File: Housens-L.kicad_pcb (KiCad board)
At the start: 4 copper layers, 50 x 50 mm, 45 parts, among them J1 JTAG/SWD, J2 USB_C_2.0, Q1 DMC3071LVT, SW1 RESET, SW2 USER_BTN, U1 MCP1603, U2 BME280, U3 OPT3005, U4 STM32WB55CGUx, Y1 32MHz, Y2 32.768kHz

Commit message: Layout JTAG
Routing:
- net /JTDI: track 0.61 -> 19.5 mm, vias 1 -> 2
- net /JTRST: track 0.61 -> 19.2 mm, vias 1 -> 2
- net /SWTRACE_JTDO: track 0.61 -> 18.5 mm, vias 1 -> 2
- net /SWCLK_JTCK: track 0.61 -> 18.4 mm, vias 1 -> 2
- net /SWDIO_JTMS: track 0.62 -> 18.2 mm, vias 1 -> 2

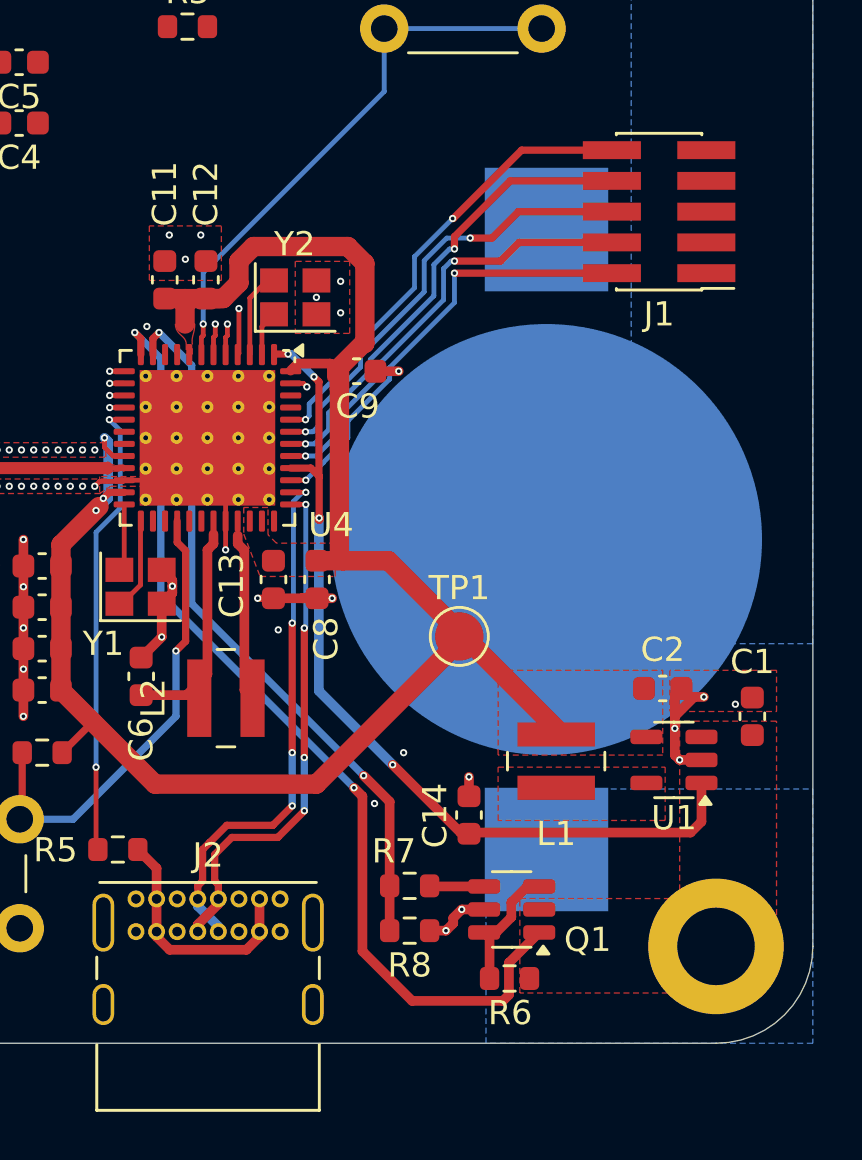
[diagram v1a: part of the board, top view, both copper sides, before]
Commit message: Add 3D model for cell holder
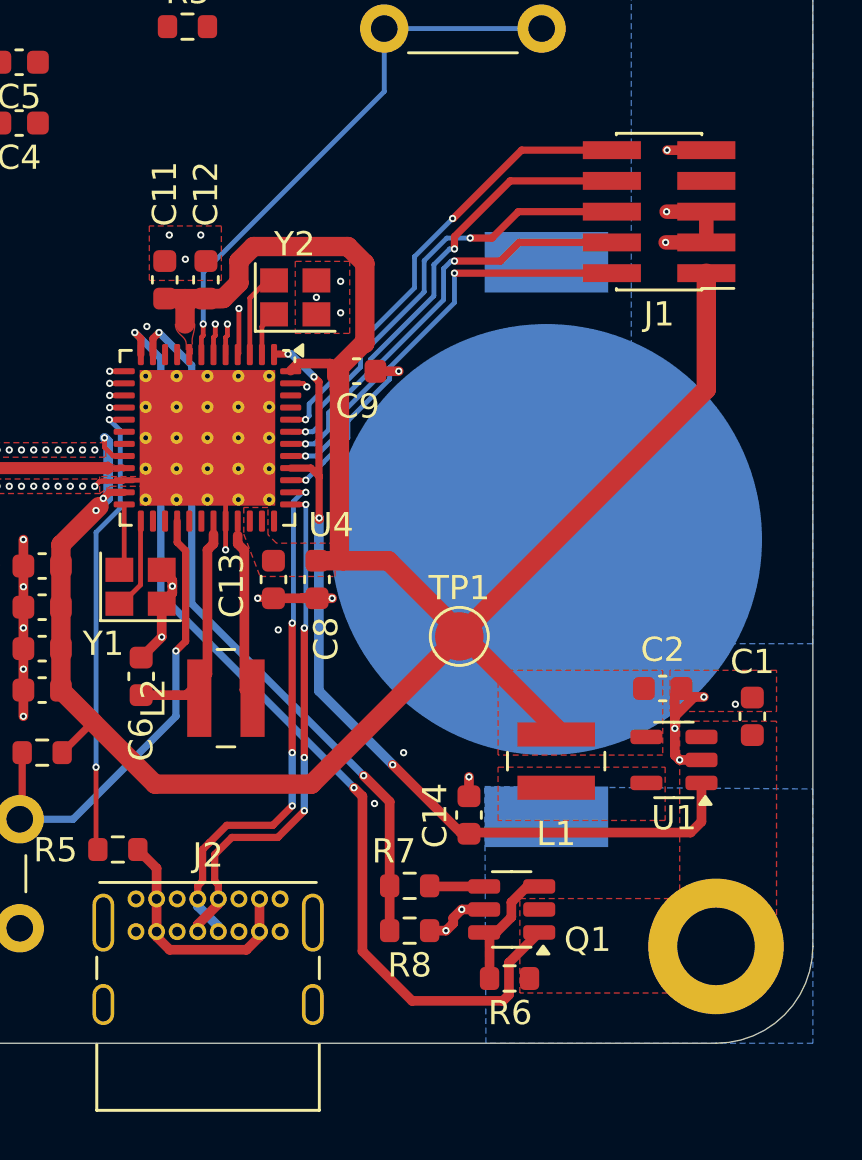
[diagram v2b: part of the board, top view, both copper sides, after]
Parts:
- BT1: footprint Battery:BatteryHolder_Keystone_3002_1x2032 -> Invented:BAT-HLD-001_3Pins
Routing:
- net +1V8: track 77.9 -> 96.9 mm
- net GND: track 36.5 -> 42.7 mm, vias 110 -> 113

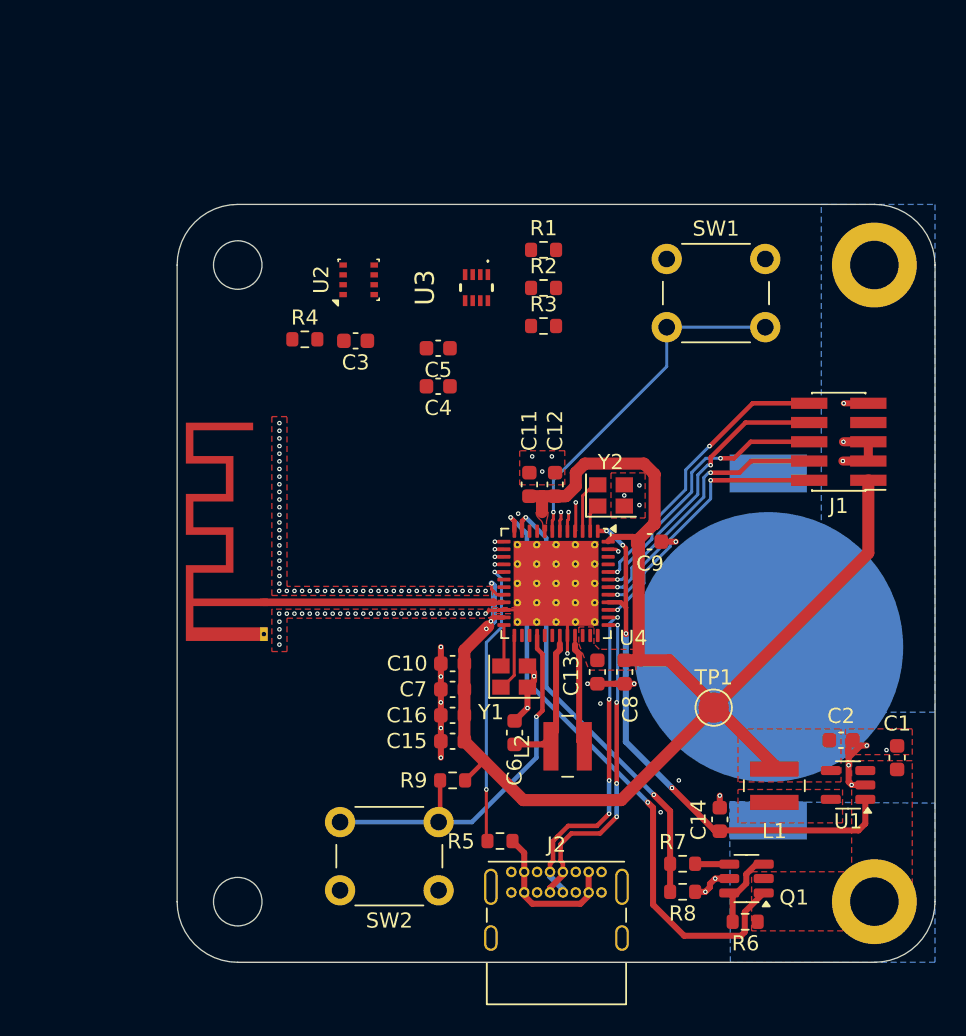
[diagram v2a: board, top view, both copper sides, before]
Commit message: Show some labels
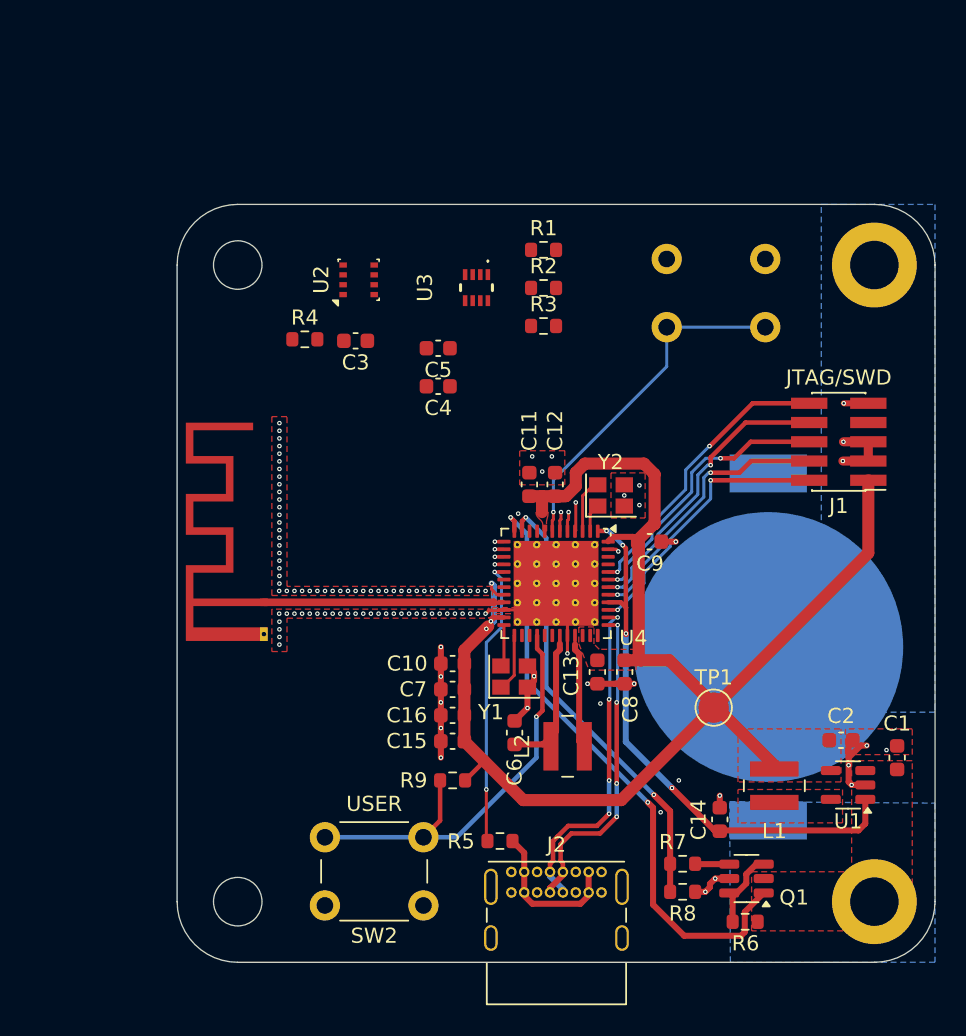
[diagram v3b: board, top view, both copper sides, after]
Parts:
- SW1: moved to B.Cu
- SW2: value USER_BTN -> USER
- moved SW1 6.50 mm to (98.8, 83.6), turned to 180 degrees
- moved SW2 1.41 mm to (76.2, 126.2)
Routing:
- net /USER_BTN: track 25.9 -> 28.7 mm

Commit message: Layout BME280
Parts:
- moved R2 27.7 mm to (59.2, 73.5)
- moved R1 27.7 mm to (59.2, 71.0)
- moved R3 27.7 mm to (59.2, 76.0)
- moved U3 27.7 mm to (54.8, 73.5)
- moved C4 27.7 mm to (52.2, 80.0)
- moved C5 27.7 mm to (52.2, 77.5)
- moved R4 17.0 mm to (84.2, 82.7), turned to 90 degrees
- moved C3 15.5 mm to (85.9, 82.7), turned to 90 degrees
- moved U2 13.1 mm to (85.0, 86.0), turned to 180 degrees
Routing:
- net +1V8: track 96.9 -> 113.7 mm
- net GND: track 42.7 -> 46.8 mm, vias 113 -> 116
- net /SPI1_MISO: track 0.60 -> 2.16 mm

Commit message: Layout I2C
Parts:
- moved SW1 29.2 mm to (72.0, 95.3), turned to -90 degrees
- moved U3 25.8 mm to (76.0, 88.1)
- moved C4 24.8 mm to (76.9, 82.7), turned to 90 degrees
- moved C5 23.5 mm to (75.2, 82.7), turned to 90 degrees
- moved R1 18.0 mm to (68.8, 86.2), turned to -90 degrees
- moved R2 17.0 mm to (70.5, 86.2), turned to -90 degrees
- moved R3 16.6 mm to (72.2, 86.2), turned to -90 degrees
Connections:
- U4 pad 4: /BOOT0 -> GND
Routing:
- net /I2C1_SDA: track 0.73 -> 28.7 mm, vias 1 -> 2
- net /I2C1_SCL: track 1.29 -> 25.3 mm, vias 1 -> 2
- net +1V8: track 113.7 -> 137.0 mm
- net /OPT_INT: track 1.29 -> 21.9 mm, vias 1 -> 2
- net Net-(U4-NRST): track 23.1 -> 16.6 mm
- net GND: track 46.8 -> 51.7 mm, vias 116 -> 122
- net /BOOT0: track 1.92 -> 0.00 mm, vias 1 -> 0

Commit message: Layout SPI
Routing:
- net /SPI1_MISO: track 2.16 -> 22.3 mm, vias 1 -> 0
- net /SPI1_MOSI: track 0.60 -> 18.8 mm, vias 1 -> 2
- net /SPI1_CLK: track 0.60 -> 17.9 mm, vias 1 -> 0
- net /SPI1_NSS: track 0.60 -> 16.9 mm, vias 1 -> 0
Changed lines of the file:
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@@
 	)
 	(via
-		(at 84.2 95.4)
-		(size 0.3)
-		(drill 0.15)
-		(layers "F.Cu" "B.Cu")
-		(remove_unused_layers yes)
-		(keep_end_layers no)
-		(zone_layer_connections "In1.Cu" "In2.Cu")
+		(at 84.1 97.1)
+		(size 0.3)
+		(drill 0.15)
+		(layers "F.Cu" "B.Cu")
+		(remove_unused_layers yes)
+		(keep_end_layers no)
+		(zone_layer_connections "F.Cu" "In1.Cu" "In2.Cu")
 		(net 2)
 	)
@@
 	)
 	(via
-		(at 84.725 96.625)
+		(at 84.6 96.55)
 		(size 0.3)
 		(drill 0.15)
@@
 	)
 	(via
-		(at 84.333364 96.366636)
+		(at 83.593199 96.55)
 		(size 0.3)
 		(drill 0.15)
@@
 	(segment
 		(start 81.5625 102.25)
-		(end 80.9625 102.25)
+		(end 81.437501 102.125001)
 		(width 0.2)
 		(layer "F.Cu")
 		(net 10)
 	)
-	(via
-		(at 80.9625 102.25)
-		(size 0.3)
-		(drill 0.15)
-		(layers "F.Cu" "B.Cu")
-		(remove_unused_layers yes)
-		(keep_end_layers no)
-		(zone_layer_connections)
+	(segment
+		(start 85.35 91.25)
+		(end 85.35 87.05)
+		(width 0.2)
+		(layer "F.Cu")
 		(net 10)
+	)
+	(segment
+		(start 81.437501 102.125001)
+		(end 81.437501 95.162499)
+		(width 0.2)
+		(layer "F.Cu")
+		(net 10)
+	)
+	(segment
+		(start 81.437501 95.162499)
+		(end 85.35 91.25)
+		(width 0.2)
+		(layer "F.Cu")
+		(net 10)
+	)
+	(segment
+		(start 81.984315 94.05)
+		(end 84.7 91.334315)
+		(width 0.2)
+		(layer "F.Cu")
+		(net 11)
+	)
+	(segment
+		(start 80.9625 101.4875)
+		(end 80.9625 95.071815)
+		(width 0.2)
+		(layer "F.Cu")
+		(net 11)
+	)
+	(segment
+		(start 80.9625 95.071815)
+		(end 81.037501 94.996814)
+		(width 0.2)
+		(layer "F.Cu")
+		(net 11)
+	)
+	(segment
+		(start 81.037501 94.996814)
+		(end 81.037501 94.996813)
+		(width 0.2)
+		(layer "F.Cu")
+		(net 11)
+	)
+	(segment
+		(start 84.7 91.334315)
+		(end 84.7 87.05)
+		(width 0.2)
+		(layer "F.Cu")
+		(net 11)
 	)
 	(segment
@@
 		(net 11)
 	)
-	(via
-		(at 80.9625 103.75)
+	(segment
+		(start 81.037501 94.996813)
+		(end 81.984315 94.05)
+		(width 0.2)
+		(layer "F.Cu")
+		(net 11)
+	)
+	(via
+		(at 80.9625 101.4875)
 		(size 0.3)
 		(drill 0.15)
@@
 		(net 11)
 	)
-	(segment
-		(start 80.9625 102.75)
-		(end 81.5625 102.75)
+	(via
+		(at 80.9625 103.75)
+		(size 0.3)
+		(drill 0.15)
+		(layers "F.Cu" "B.Cu")
+		(remove_unused_layers yes)
+		(keep_end_layers no)
+		(zone_layer_connections)
+		(net 11)
+	)
+	(segment
+		(start 80.9625 101.4875)
+		(end 80.9625 103.75)
+		(width 0.2)
+		(layer "B.Cu")
+		(net 11)
+	)
+	(segment
+		(start 81.110614 102.75)
+		(end 80.5125 102.151886)
 		(width 0.2)
 		(layer "F.Cu")
 		(net 12)
 	)
-	(via
-		(at 80.9625 102.75)
-		(size 0.3)
-		(drill 0.15)
-		(layers "F.Cu" "B.Cu")
-		(remove_unused_layers yes)
-		(keep_end_layers no)
-		(zone_layer_connections)
+	(segment
+		(start 80.5125 102.151886)
+		(end 80.5125 94.956129)
+		(width 0.2)
+		(layer "F.Cu")
 		(net 12)
+	)
+	(segment
+		(start 81.5625 102.75)
+		(end 81.110614 102.75)
+		(width 0.2)
+		(layer "F.Cu")
+		(net 12)
+	)
+	(segment
+		(start 80.5125 94.956129)
+		(end 84.05 91.418629)
+		(width 0.2)
+		(layer "F.Cu")
+		(net 12)
+	)
+	(segment
+		(start 84.05 91.418629)
+		(end 84.05 87.05)
+		(width 0.2)
+		(layer "F.Cu")
+		(net 12)
+	)
+	(segment
+		(start 80.1125 102.317572)
+		(end 80.1125 94.790443)
+		(width 0.2)
+		(layer "F.Cu")
+		(net 13)
 	)
 	(segment
@@
 	)
 	(segment
-		(start 80.9625 103.25)
-		(end 81.5625 103.25)
+		(start 80.1125 94.790443)
+		(end 83.351472 91.551471)
+		(width 0.2)
+		(layer "F.Cu")
+		(net 13)
+	)
+	(segment
+		(start 83.351472 85.698528)
+		(end 84.05 85)
+		(width 0.2)
+		(layer "F.Cu")
+		(net 13)
+	)
+	(segment
+		(start 83.351472 91.551471)
+		(end 83.351472 85.698528)
+		(width 0.2)
+		(layer "F.Cu")
+		(net 13)
+	)
+	(segment
+		(start 81.044928 103.25)
+		(end 80.1125 102.317572)
+		(width 0.2)
+		(layer "F.Cu")
+		(net 13)
+	)
+	(segment
+		(start 81.5625 103.25)
+		(end 81.044928 103.25)
 		(width 0.2)
 		(layer "F.Cu")
@@
 		(net 13)
 	)
-	(via
-		(at 80.9625 103.25)
-		(size 0.3)
-		(drill 0.15)
-		(layers "F.Cu" "B.Cu")
-		(remove_unused_layers yes)
-		(keep_end_layers no)
-		(zone_layer_connections)
-		(net 13)
-	)

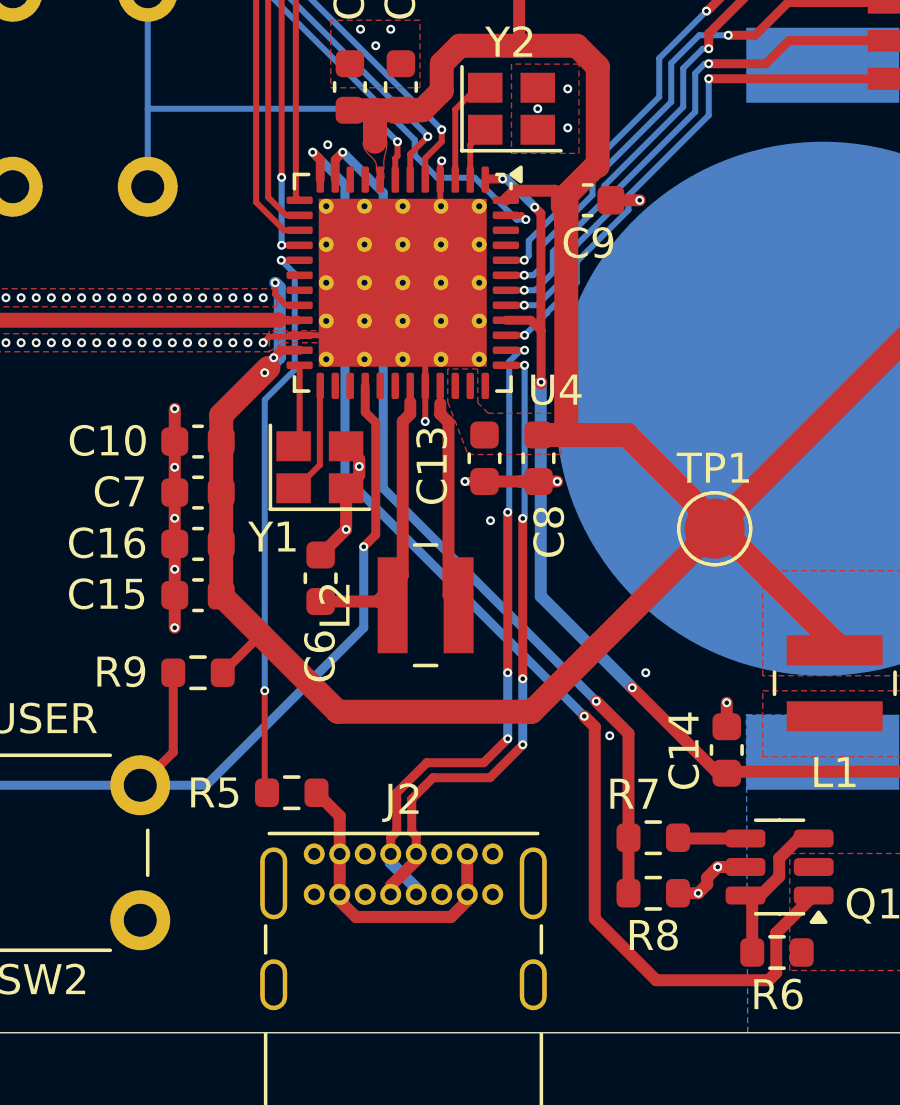
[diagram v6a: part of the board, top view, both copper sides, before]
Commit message: Impedance-match USB lines
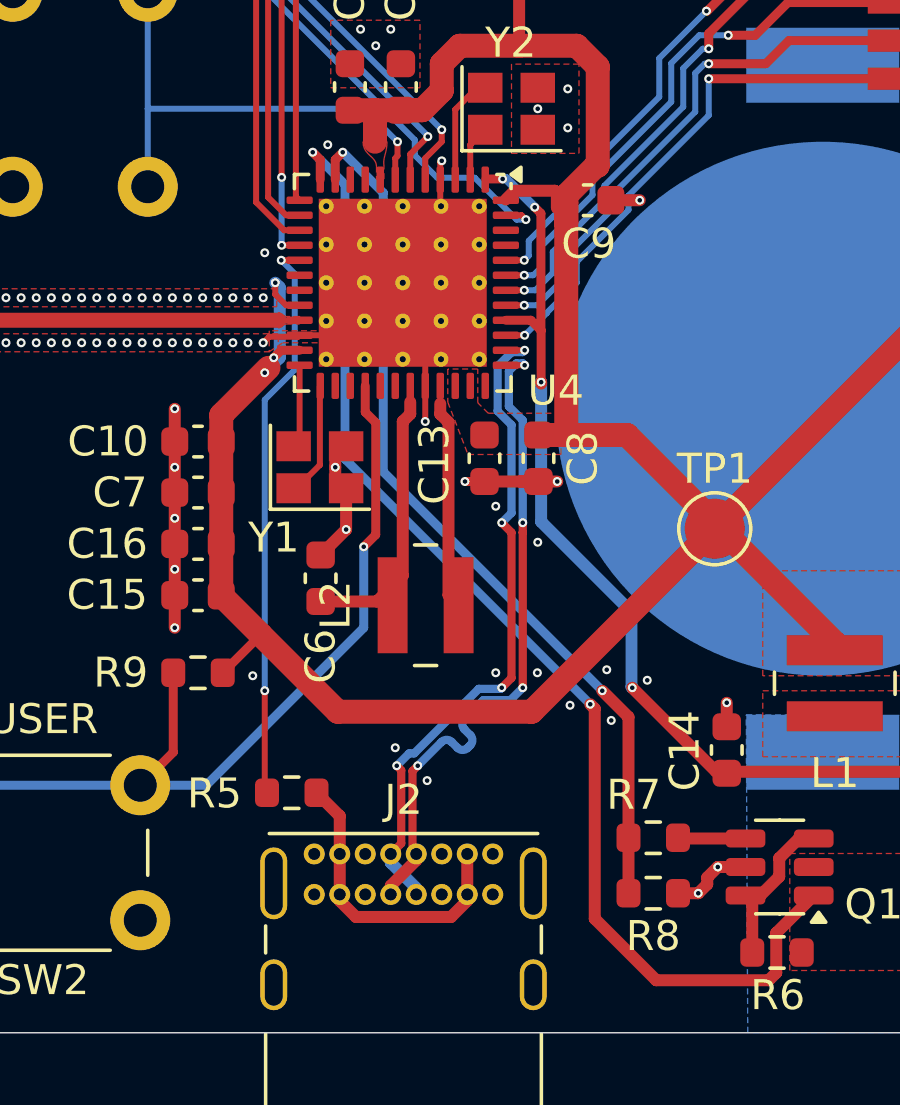
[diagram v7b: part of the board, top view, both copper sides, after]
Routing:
- net /USB_D_N: track 21.4 -> 22.4 mm
- net GND: vias 122 -> 131

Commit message: Stitch and finalise labels
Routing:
- net GND: vias 131 -> 208
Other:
- board text added: "serial number barcode"
